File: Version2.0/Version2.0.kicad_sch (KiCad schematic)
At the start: 3 parts, among them U1 DS3231M, U2 ESP-12F, U3 TMP36xS

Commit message: electrical design
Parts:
- removed U1: DS3231M, Package_SO:SOIC-16W_7.5x10.3mm_P1.27mm, symbol Timer_RTC:DS3231M
- removed U3: TMP36xS, Package_SO:SOIC-8_3.9x4.9mm_P1.27mm, symbol Sensor_Temperature:TMP36xS
- added C1: 100nF, symbol Device:C
- added C2: 100uF, symbol Device:C
- added C3: 10uF, symbol Device:C
- added R1: 150k, symbol Device:R
- added R2: 470k, symbol Device:R
- added R3, R4, R5: 10k, symbol Device:R
- added STEMMA1: JST_SH_1.0mm_5pin, Connector_JST:JST_SH_BM05B-SRSS-TB_1x05-1MP_P1.00mm_Vertical, symbol Connector:Conn_01x05_Pin
- added SW1: SW_Push, symbol Switch:SW_Push
- added U1: DS3231MZ, Package_SO:SOIC-8_3.9x4.9mm_P1.27mm, symbol Timer_RTC:DS3231MZ
- added U3: ~, symbol TP4056_sym:TP4056_Module
- added U4: HT75xx-1-SOT89, Package_TO_SOT_SMD:SOT-89-3, symbol Regulator_Linear:HT75xx-1-SOT89
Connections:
- net +3.3V: now also C2.1, R3.1, R5.1, STEMMA1.1 (Pin_1), U1.6 (VBAT), U4.3 (VOUT)
- net GND: now also C2.2, C3.2, R1.2, R4.2, STEMMA1.5 (Pin_5), SW1.1, U1.5 (GND), U3.4 (OUT-), U4.1 (GND)
- net RST: now reaches U2.1 (~{RST})
- net RST: now also C1.2, SW1.2
- net at U2.16 (GPIO15): now also R4.1
- net at U2.17 (GPIO2): now also R5.2
- net Flash: now reaches U2.18 (GPIO0)
- net Flash: now also STEMMA1.2 (Pin_2)
- net SDA: now reaches U2.19 (GPIO4)
- net SDA: now also U1.7 (SDA)
- net A0: now reaches U2.2 (ADC)
- net A0: now also R1.1, R2.2
- net SCL: now reaches U2.20 (GPIO5)
- net SCL: now also U1.8 (SCL)
- net RX: now reaches U2.21 (GPIO3/RXD)
- net RX: now also STEMMA1.4 (Pin_4)
- net TX: now reaches U2.22 (GPIO1/TXD)
- net TX: now also STEMMA1.3 (Pin_3)
- net at U2.3 (EN): now also R3.2
- new net: C1.1, U1.3 (~{INT}/SQW)
- new net VBATT+: U3.5 (B+)
- new net VBATT-: U3.6 (B-)
- new net VCC: C3.1, R2.1, U3.3 (OUT+), U4.2 (VIN)
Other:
- note added: "Battery Level Indicator"
- note added: "Charging Circuit"
- note added: "For Firmware Flash"
- note added: "Micro Controller"
- note added: "RTC"
- note added: "Stemma Connectors"
- note added: "Voltage Regulator"
- company: (none) -> Incepta Pharmaceuticals
- title: (none) -> OpenLogger Schematics
- moved on the sheet: U2

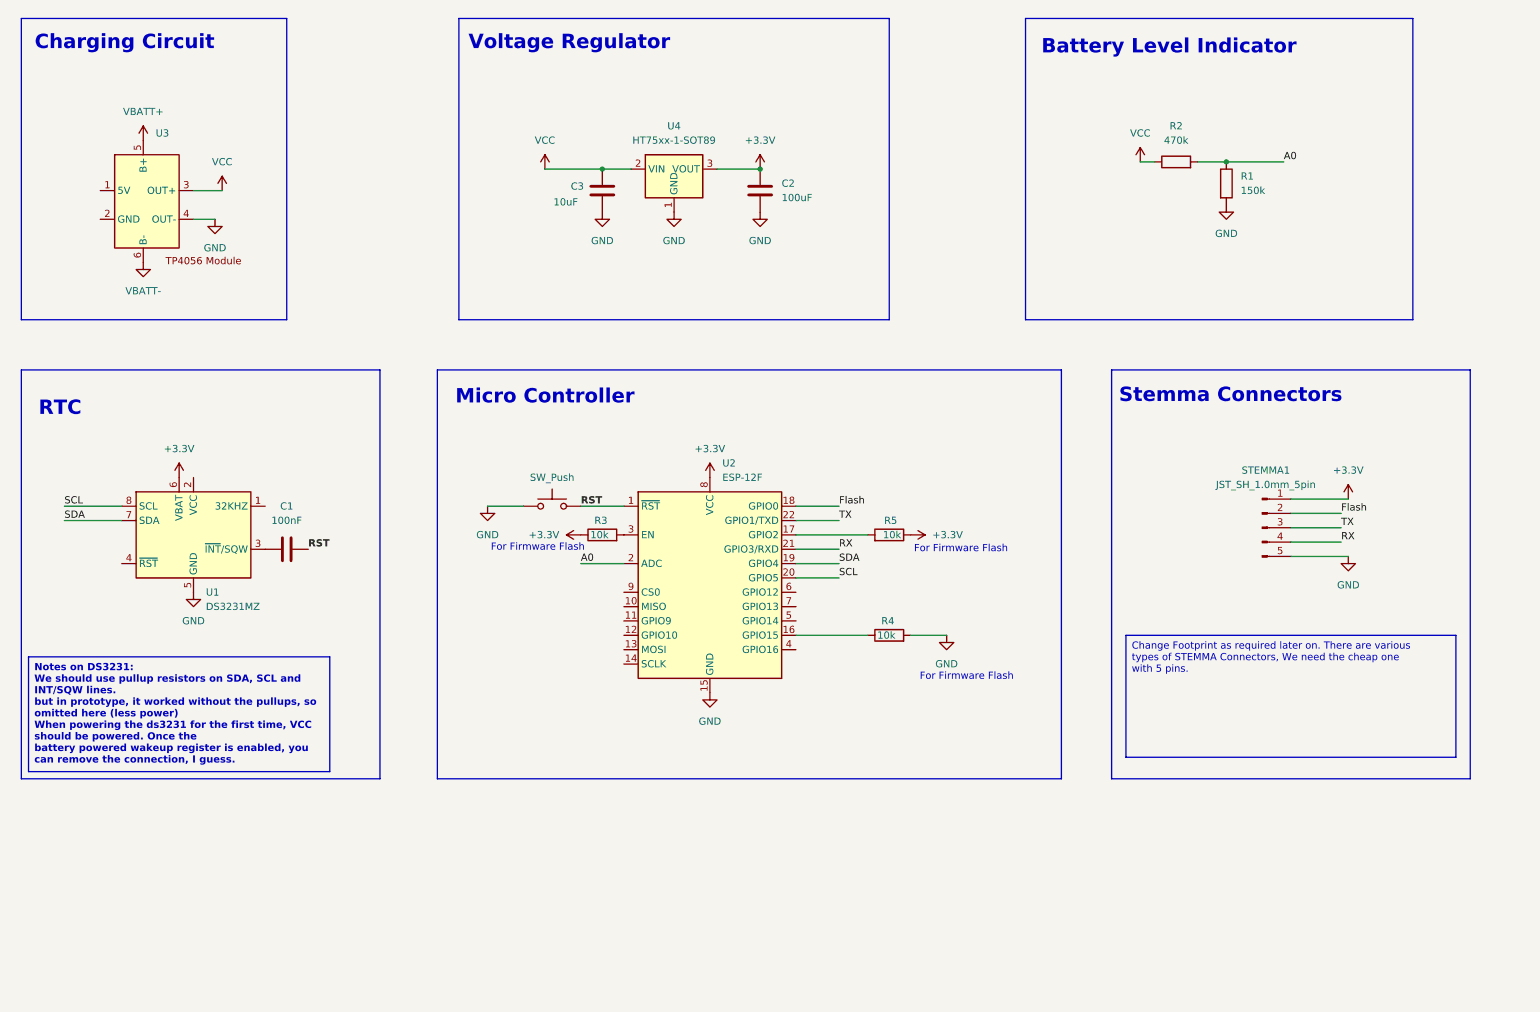
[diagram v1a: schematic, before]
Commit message: Schematics Update
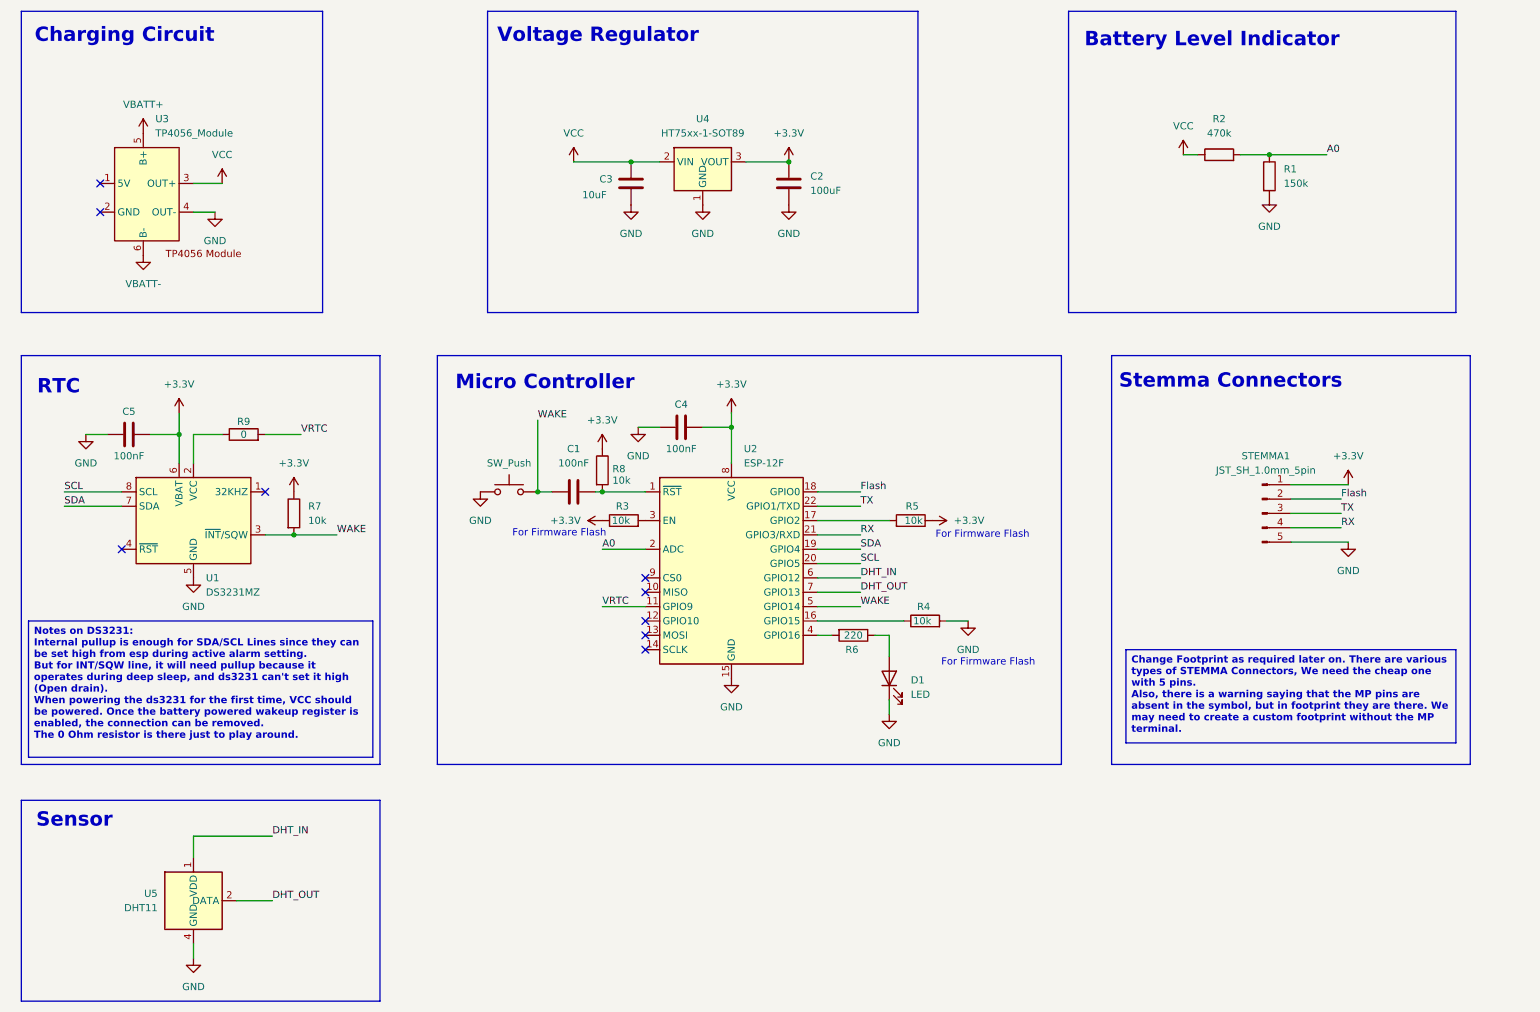
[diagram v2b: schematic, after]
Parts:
- added C4, C5: 100nF, Capacitor_SMD:C_0805_2012Metric, symbol Device:C
- added D1: LED, LED_SMD:LED_0805_2012Metric, symbol Device:LED
- added R6: 220, Resistor_SMD:R_0805_2012Metric, symbol Device:R
- added R7, R8: 10k, symbol Device:R
- added R9: 0, symbol Device:R
- added U5: DHT11, Sensor:Aosong_DHT11_5.5x12.0_P2.54mm, symbol Sensor:DHT11
- C1: footprint (none) -> Capacitor_SMD:C_0805_2012Metric
- C2, C3: footprint (none) -> Capacitor_SMD:C_1210_3225Metric
- R1, R2, R3, R4, R5: footprint (none) -> Resistor_SMD:R_0805_2012Metric
- SW1: footprint (none) -> Button_Switch_THT:SW_PUSH_6mm
- U3: value ~ -> TP4056_Module; footprint (none) -> TP4056:TP4056-18650
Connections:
- net +3.3V: now also C4.2, C5.2, R7.1, R8.1
- net GND: now also C4.1, C5.1, D1.1 (K), U5.4 (GND)
- net VRTC: now reaches U2.11 (GPIO9)
- net VRTC: now also R9.2
- net at U2.4 (GPIO16): now also R6.2
- net WAKE: now reaches U2.5 (GPIO14)
- net WAKE: now also C1.1, SW1.2, U1.3 (~{INT}/SQW), R7.2
- net DHT_IN: now reaches U2.6 (GPIO12)
- net DHT_IN: now also U5.1 (VDD)
- net DHT_OUT: now reaches U2.7 (GPIO13)
- net DHT_OUT: now also U5.2 (DATA)
- net at U1.2 (VCC): now also R9.1
- net RST: no longer names the net of C1.2, U2.1 (~{RST})
- net RST: now also R8.2; no longer SW1.2
- new net: D1.2 (A), R6.1
- no-connect marks 0 -> 9
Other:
- note added: "Sensor"
- moved on the sheet: C1, C2, C3, R1, R2, R3, R4, R5, STEMMA1, U1, U2, U3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

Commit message: PCB Design
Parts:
- removed C2: 100uF, Capacitor_SMD:C_1210_3225Metric, symbol Device:C
- R7, R8, R9: footprint (none) -> Resistor_SMD:R_0805_2012Metric
- STEMMA1: footprint Connector_JST:JST_SH_BM05B-SRSS-TB_1x05-1MP_P1.00mm_Vertical -> Connector_JST:JST_XH_B5B-XH-A_1x05_P2.50mm_Vertical
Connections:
- net VRTC: now also U2.4 (GPIO16); no longer U2.11 (GPIO9)
- net at R6.2: now also U2.11 (GPIO9); no longer U2.4 (GPIO16)
